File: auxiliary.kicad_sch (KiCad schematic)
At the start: 32 parts, among them J7 Conn_01x05, J9 Conn_02x06_Odd_Even, U6 PCA9554APW, Y1 32.768KHZ, Y2 X322525MOB4SI-25MHz

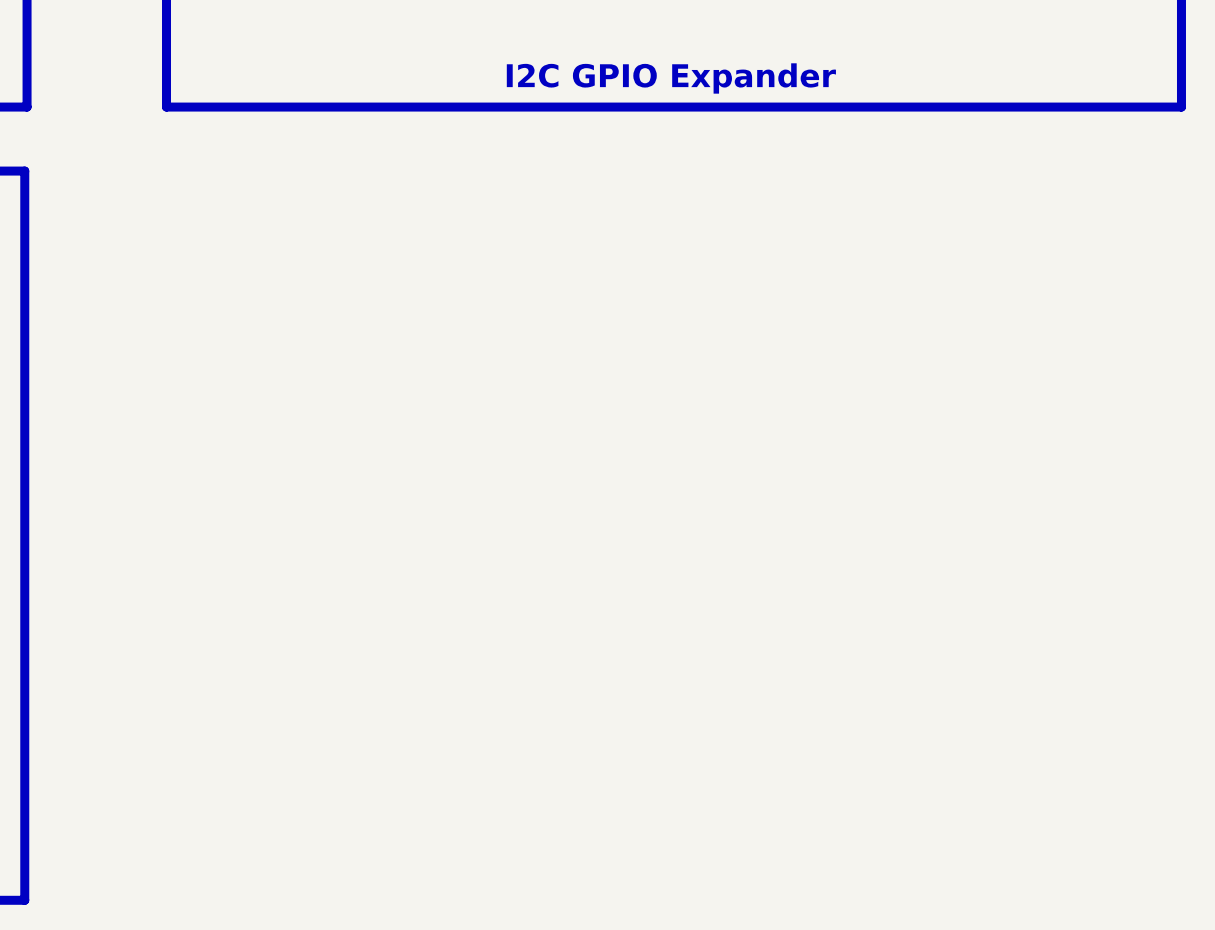
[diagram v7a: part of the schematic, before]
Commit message: added fiducal markers, mounting holes, testpoints
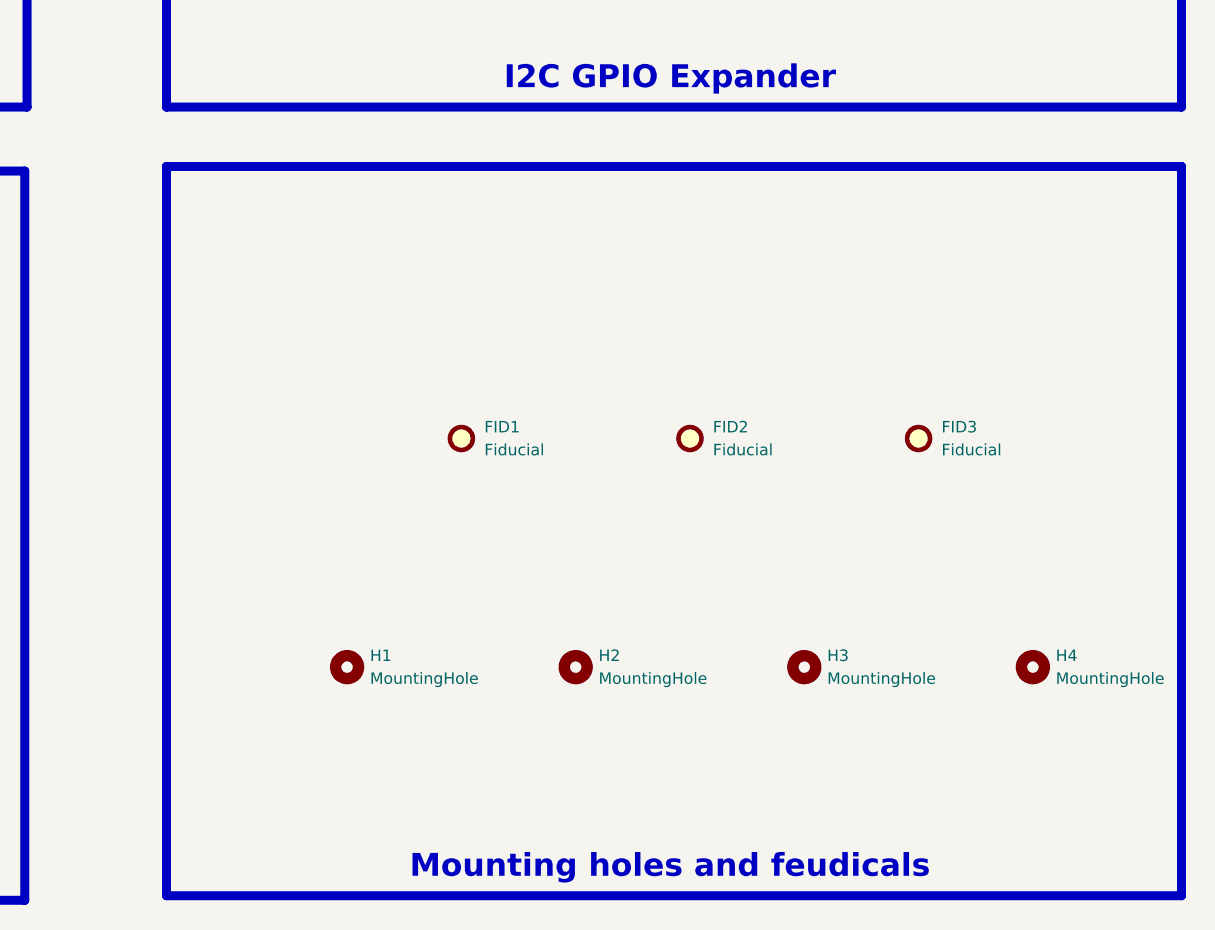
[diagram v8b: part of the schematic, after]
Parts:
- added FID1, FID2, FID3: Fiducial, 0_pads:Fiducial_1mm_Mask2mm, symbol Mechanical:Fiducial
- added H1, H2, H3, H4: MountingHole, MountingHole:MountingHole_3.2mm_M3_DIN965_Pad, symbol Mechanical:MountingHole
